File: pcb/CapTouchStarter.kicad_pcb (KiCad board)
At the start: 2 copper layers, 73.5 x 64 mm, 44 parts, among them J1 USB_C_Receptacle, J2 62684-50110, Q1 SS8050-G, Q2 SS8050-G, SW1 BOOT, SW2 EN, U1 1965-ESP32-WROOM-32E(8MB)CT-ND, U2 AMS1117-3.3, U3 CP2102N-A01-GQFN28

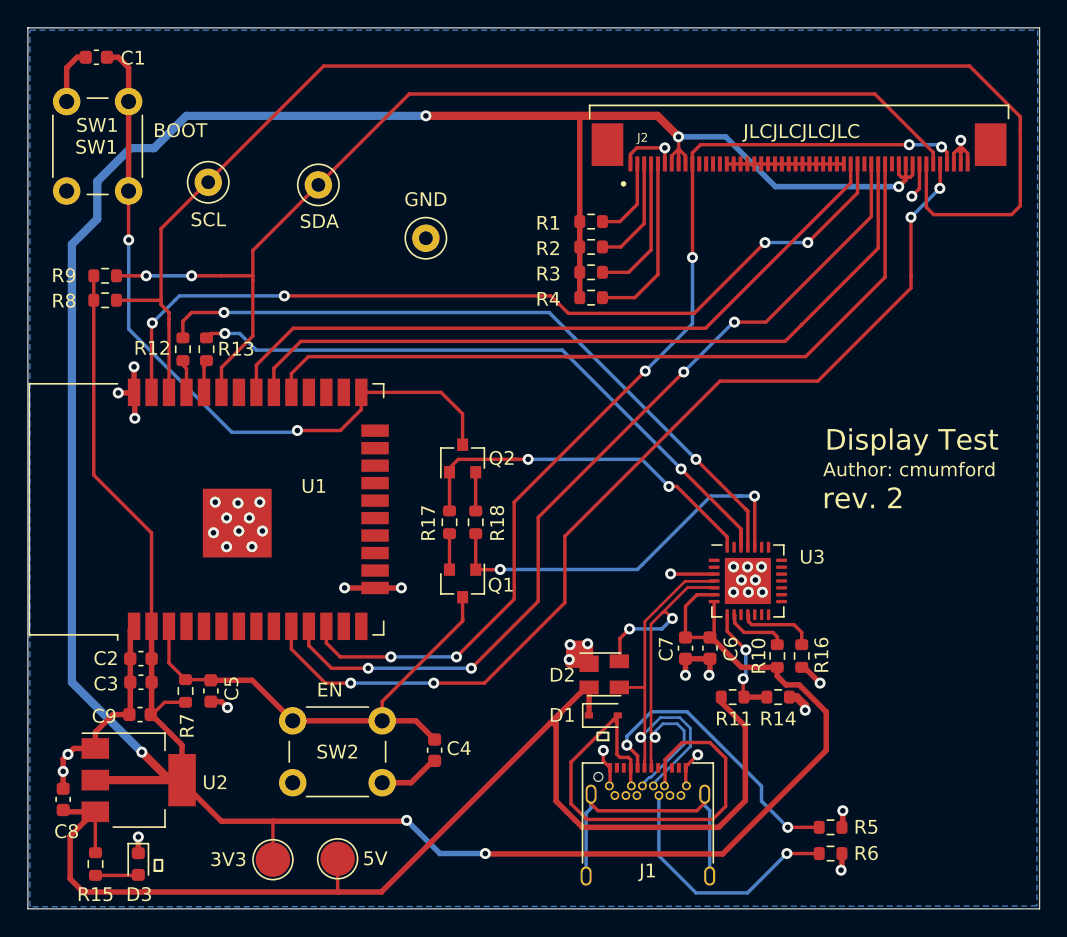
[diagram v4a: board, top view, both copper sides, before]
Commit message: Corrected LCD pin order.
The 50-pin flat pack ribbon cable has reversed pin ordering.
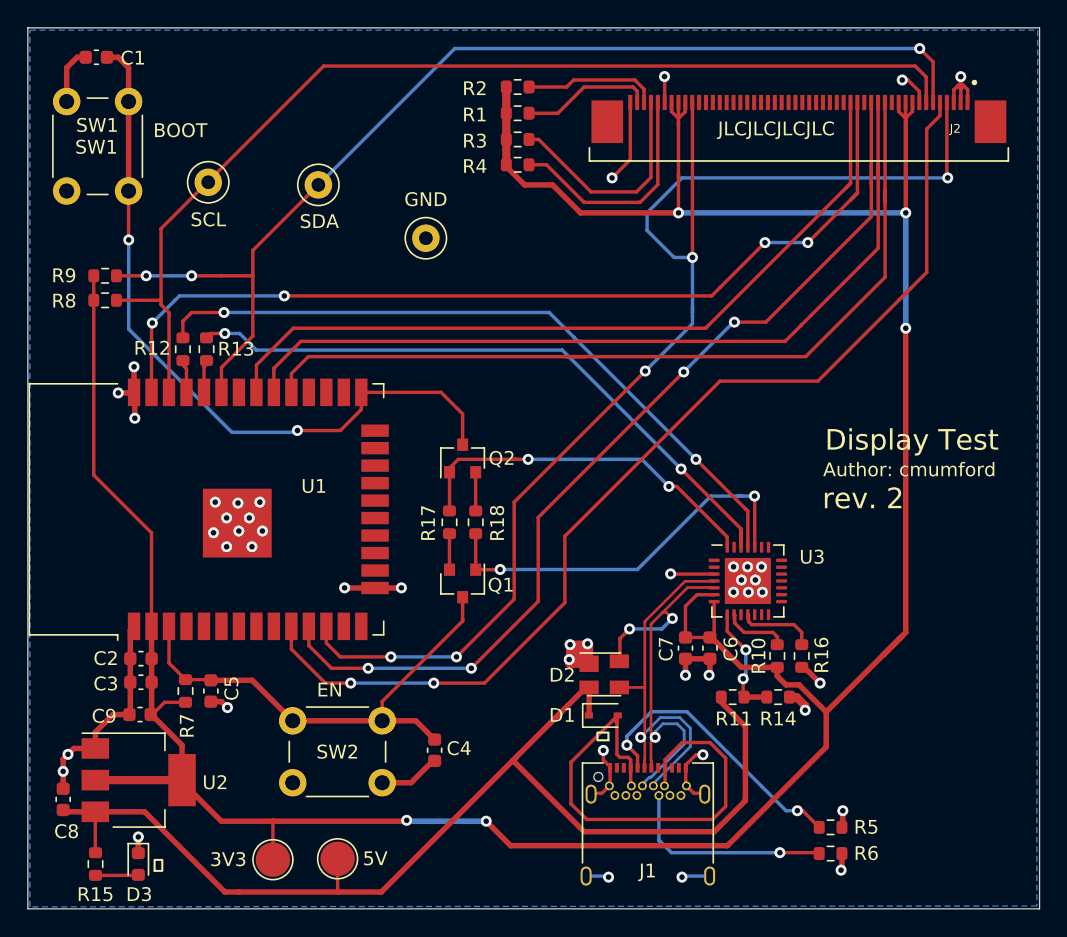
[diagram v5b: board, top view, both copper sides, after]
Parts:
- moved R2 12.8 mm to (164.1, 82.3)
- moved R3 11.0 mm to (164.1, 86.1)
- moved R4 11.0 mm to (164.1, 87.9)
- moved R1 9.51 mm to (164.1, 84.2)
- moved J2 1.28 mm to (185.1, 85.4), turned to 270 degrees
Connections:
- J1 pad S1: Net-(J1-PadS1) -> GND
- J2 pad 10: Net-(J2-Pad10) -> +3V3
- J2 pad 11: Net-(J2-Pad11) -> +3V3
- J2 pad 16: Net-(J2-Pad15) -> Net-(J2-Pad16)
- J2 pad 17: Net-(J2-Pad15) -> Net-(J2-Pad17)
- J2 pad 18: Net-(J2-Pad15) -> Net-(J2-Pad18)
- J2 pad 19: Net-(J2-Pad15) -> Net-(J2-Pad19)
- J2 pad 2: Net-(J2-Pad2) -> GND
- J2 pad 20: Net-(J2-Pad15) -> Net-(J2-Pad20)
- J2 pad 21: Net-(J2-Pad15) -> Net-(J2-Pad21)
- J2 pad 22: Net-(J2-Pad15) -> Net-(J2-Pad22)
- J2 pad 23: Net-(J2-Pad15) -> Net-(J2-Pad23)
- J2 pad 24: Net-(J2-Pad15) -> Net-(J2-Pad24)
- J2 pad 25: Net-(J2-Pad15) -> Net-(J2-Pad25)
- J2 pad 26: Net-(J2-Pad15) -> Net-(J2-Pad26)
- J2 pad 27: Net-(J2-Pad15) -> Net-(J2-Pad27)
- J2 pad 28: Net-(J2-Pad15) -> Net-(J2-Pad28)
- J2 pad 29: Net-(J2-Pad15) -> Net-(J2-Pad29)
- J2 pad 3: Net-(J2-Pad3) -> GND
- J2 pad 30: Net-(J2-Pad15) -> Net-(J2-Pad30)
- J2 pad 31: Net-(J2-Pad15) -> Net-(J2-Pad31)
- J2 pad 32: Net-(J2-Pad15) -> Net-(J2-Pad32)
- J2 pad 40: +3V3 -> Net-(J2-Pad40)
- J2 pad 41: +3V3 -> Net-(J2-Pad4)
- J2 pad 43: GND -> +3V3
- J2 pad 44: Net-(J2-Pad44) -> +3V3
- J2 pad 45: Net-(J2-Pad45) -> GND
- J2 pad 47: Net-(J2-Pad10) -> Net-(J2-Pad47)
- J2 pad 48: GND -> Net-(J2-Pad48)
- J2 pad 49: GND -> Net-(J2-Pad49)
- J2 pad 6: GND -> Net-(J2-Pad6)
- J2 pad 7: +3V3 -> Net-(J2-Pad7)
- J2 pad 8: +3V3 -> GND
- R1 pad 1: Net-(J2-Pad2) -> Net-(J2-Pad49)
- R2 pad 1: Net-(J2-Pad3) -> Net-(J2-Pad48)
- R3 pad 1: Net-(J2-Pad4) -> Net-(J2-Pad47)
- R4 pad 1: Net-(J2-Pad5) -> Net-(J2-Pad46)
- R8 pad 2: Net-(J2-Pad44) -> Net-(J2-Pad7)
- R9 pad 2: Net-(J2-Pad45) -> Net-(J2-Pad6)
- TP2 pad 1: Net-(J2-Pad44) -> Net-(J2-Pad7)
- TP3 pad 1: Net-(J2-Pad45) -> Net-(J2-Pad6)
- U1 pad 10: Net-(J2-Pad46) -> Net-(J2-Pad5)
- U1 pad 11: Net-(J2-Pad36) -> Net-(J2-Pad15)
- U1 pad 12: Net-(J2-Pad10) -> Net-(J2-Pad4)
- U1 pad 29: Net-(J2-Pad38) -> Net-(J2-Pad13)
- U1 pad 30: Net-(J2-Pad37) -> Net-(J2-Pad14)
- U1 pad 31: Net-(J2-Pad33) -> Net-(J2-Pad18)
- U1 pad 33: Net-(J2-Pad45) -> Net-(J2-Pad6)
- U1 pad 36: Net-(J2-Pad44) -> Net-(J2-Pad7)
- U1 pad 37: Net-(J2-Pad34) -> Net-(J2-Pad17)
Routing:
- net Net-(J2-Pad44): track 101.1 -> 0.00 mm
- net Net-(J2-Pad4): track 10.5 -> 92.9 mm, vias 0 -> 5
- net Net-(J2-Pad6): track 0.00 -> 80.0 mm, vias 0 -> 3
- net Net-(J2-Pad7): track 0.00 -> 78.0 mm
- net Net-(J2-Pad45): track 77.9 -> 0.00 mm, vias 2 -> 0
- net Net-(J2-Pad10): track 75.1 -> 0.00 mm, vias 6 -> 0
- net Net-(J2-Pad17): track 0.00 -> 67.5 mm, vias 0 -> 4
- net Net-(J2-Pad5): track 12.8 -> 78.0 mm, vias 0 -> 2
- net Net-(J2-Pad36): track 64.1 -> 0.00 mm, vias 4 -> 0
- net Net-(J2-Pad34): track 63.4 -> 0.00 mm, vias 4 -> 0
- net Net-(J2-Pad13): track 0.00 -> 63.1 mm
- net Net-(J2-Pad15): track 8.50 -> 70.1 mm, vias 0 -> 4
- net Net-(J2-Pad14): track 0.00 -> 61.1 mm
- net Net-(J2-Pad38): track 57.8 -> 0.00 mm
- net Net-(J2-Pad18): track 0.00 -> 57.0 mm
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
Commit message: Removed 0Ω TX/RX resistors.
Also minor routing cleanup.
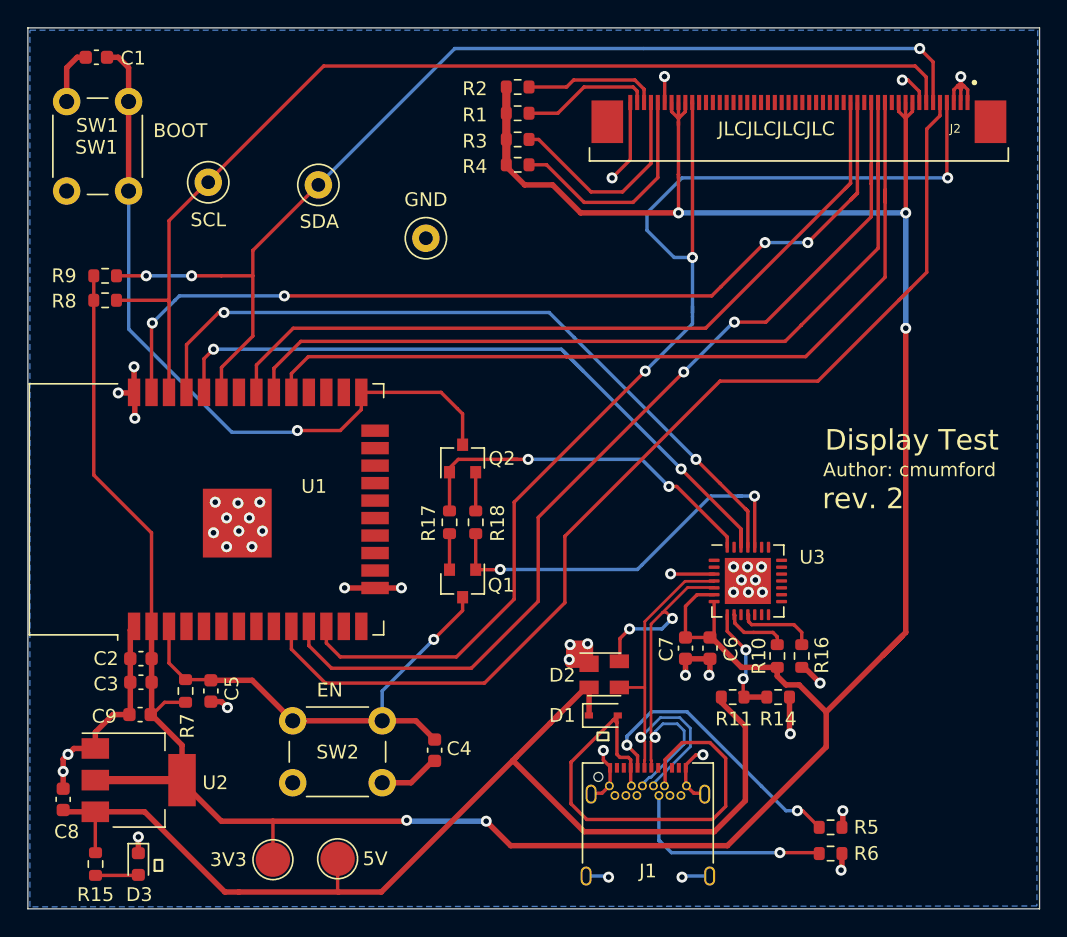
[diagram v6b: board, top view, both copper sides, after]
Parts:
- removed R12, R13: 0Ω, Resistor_SMD:R_0603_1608Metric
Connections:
- U3 pad 25: Net-(R12-Pad2) -> TXD
- U3 pad 26: Net-(R13-Pad2) -> RXD
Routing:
- net TXD: track 2.42 -> 54.0 mm, vias 0 -> 2
- net Net-(R12-Pad2): track 51.3 -> 0.00 mm, vias 2 -> 0
- net RXD: track 2.38 -> 51.8 mm, vias 0 -> 2
- net Net-(R13-Pad2): track 47.4 -> 0.00 mm, vias 2 -> 0
- net GND: track 87.5 -> 88.4 mm
- net Net-(J2-Pad47): track 16.3 -> 15.7 mm
- net EN: track 35.9 -> 35.7 mm, vias 0 -> 1
- net Net-(J2-Pad5): vias 2 -> 0
- net Net-(J2-Pad4): vias 5 -> 3
- net Net-(J2-Pad15): vias 4 -> 2
- net IO0: vias 2 -> 1

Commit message: Added TX/RX LED's.
Also, layout cleanup.
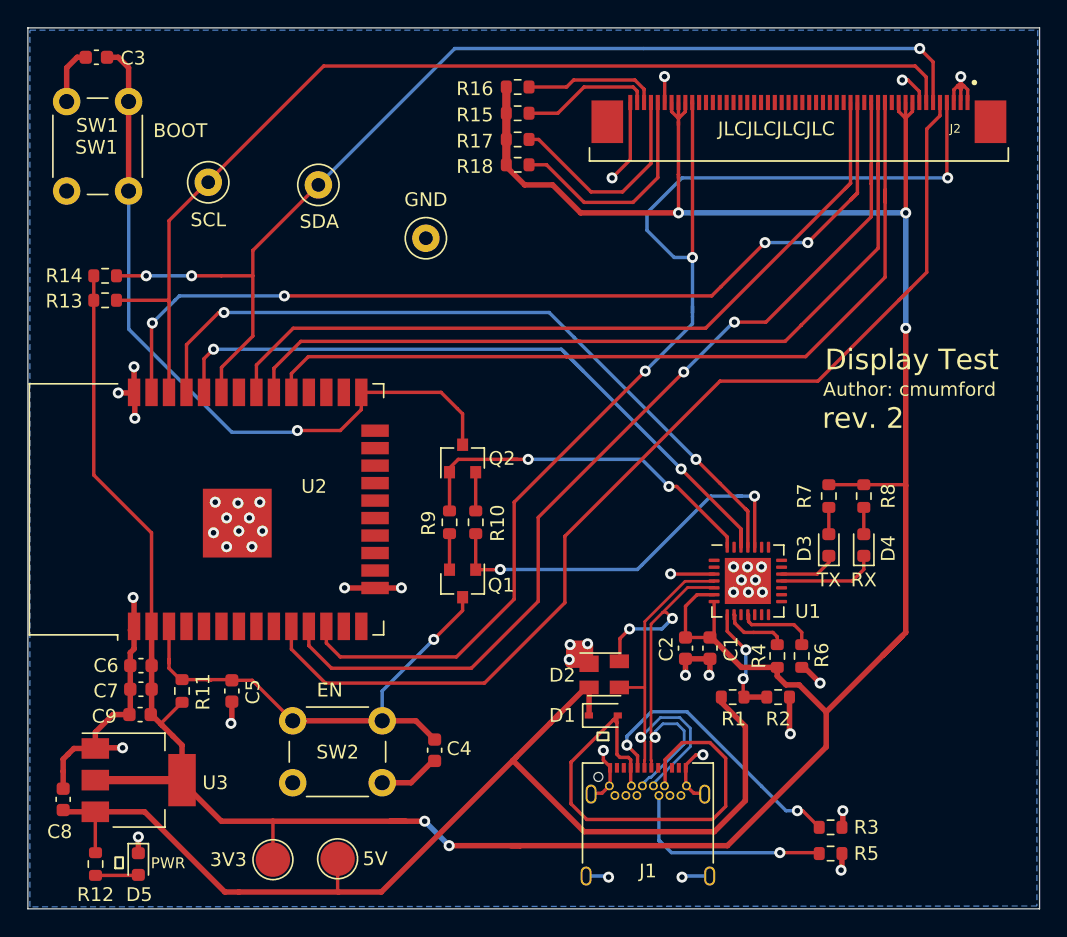
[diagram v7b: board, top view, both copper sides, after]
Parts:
- removed the U1 at (144.5, 113.0)
- added D3: TX, LED_SMD:LED_0603_1608Metric, F.Cu at (186.7, 115.6)
- added D4: RX, LED_SMD:LED_0603_1608Metric, F.Cu at (189.2, 115.6)
- added R7: 2KΩ, Resistor_SMD:R_0603_1608Metric, F.Cu at (186.7, 112.0)
- added R8: 2KΩ, Resistor_SMD:R_0603_1608Metric, F.Cu at (189.2, 112.0)
- added U2: 1965-ESP32-WROOM-32E(8MB)CT-ND, RF_Module:ESP32-WROOM-32, F.Cu at (144.5, 113.0)
- D5: renamed from D3; value LED (red) -> PWR
- moved C5 1.52 mm to (143.3, 126.2)
- moved C6 0.51 mm to (136.7, 124.3)
- moved C7 0.51 mm to (136.7, 126.0)
- moved R11 0.25 mm to (139.7, 126.2)
- renumbered C6 to C1, C7 to C2, C1 to C3, C2 to C6, C3 to C7, R11 to R1, R18 to R10, R7 to R11, R15 to R12, R8 to R13, R9 to R14, R1 to R15, R2 to R16, R3 to R17, R4 to R18, R14 to R2, R5 to R3, R10 to R4, R6 to R5, R16 to R6, R17 to R9, TP4 to TP2, TP5 to TP3, TP2 to TP4, TP3 to TP5, U3 to U1, U2 to U3
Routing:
- net Net-(D4-Pad1): track 0.00 -> 7.31 mm
- net +3V3: track 226.2 -> 232.9 mm
- net GND: track 88.4 -> 93.1 mm
- net Net-(D3-Pad1): track 0.00 -> 4.26 mm
- net Net-(D4-Pad2): track 0.00 -> 1.94 mm
- net Net-(D3-Pad2): track 0.00 -> 1.94 mm

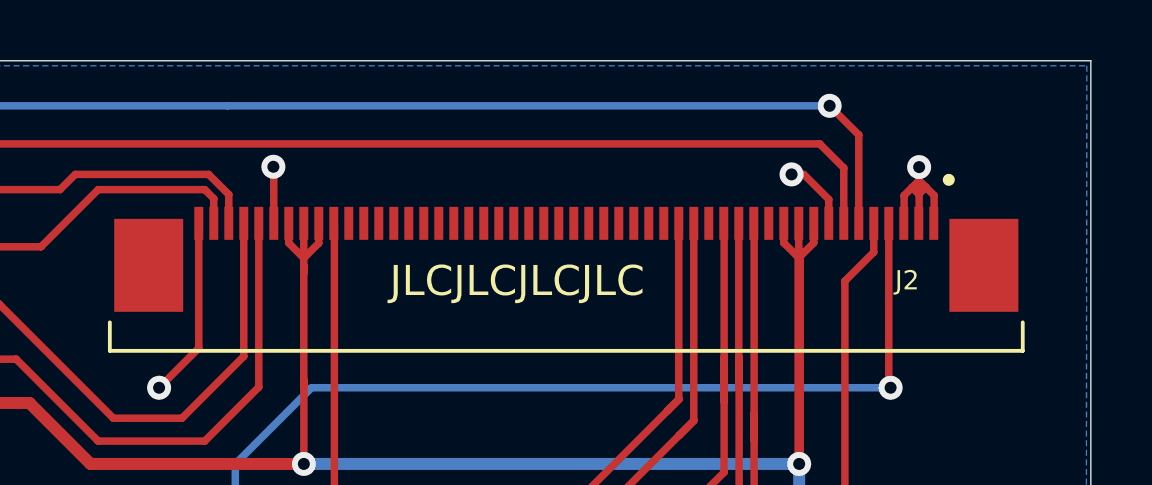
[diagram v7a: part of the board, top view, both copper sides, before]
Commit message: Added display silkscreen pin numbers.
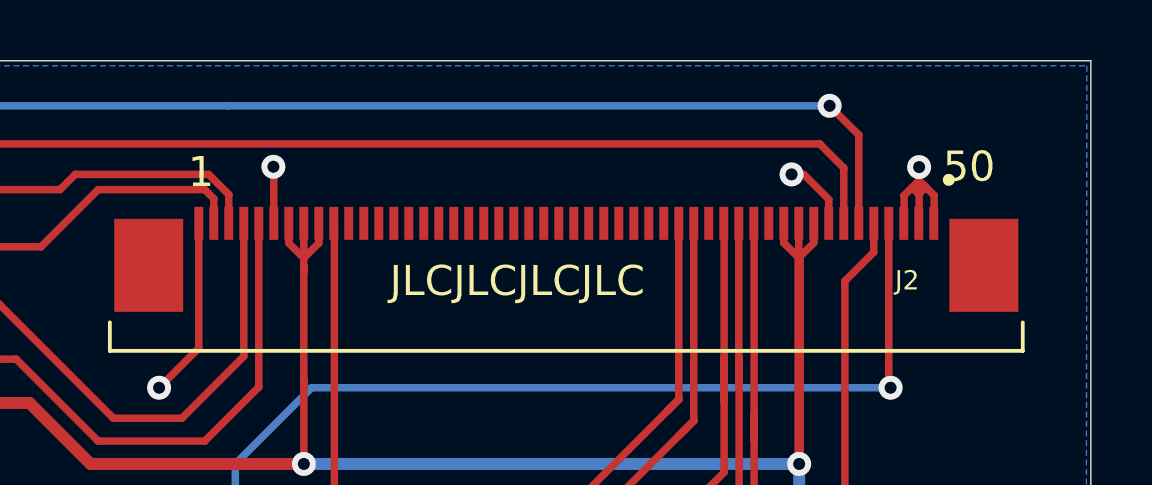
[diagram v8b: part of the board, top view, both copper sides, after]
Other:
- board text added: "1"
- board text added: "50"
